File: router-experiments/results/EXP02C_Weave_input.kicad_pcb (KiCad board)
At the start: 2 copper layers, 45.4 x 45.4 mm, 144 parts

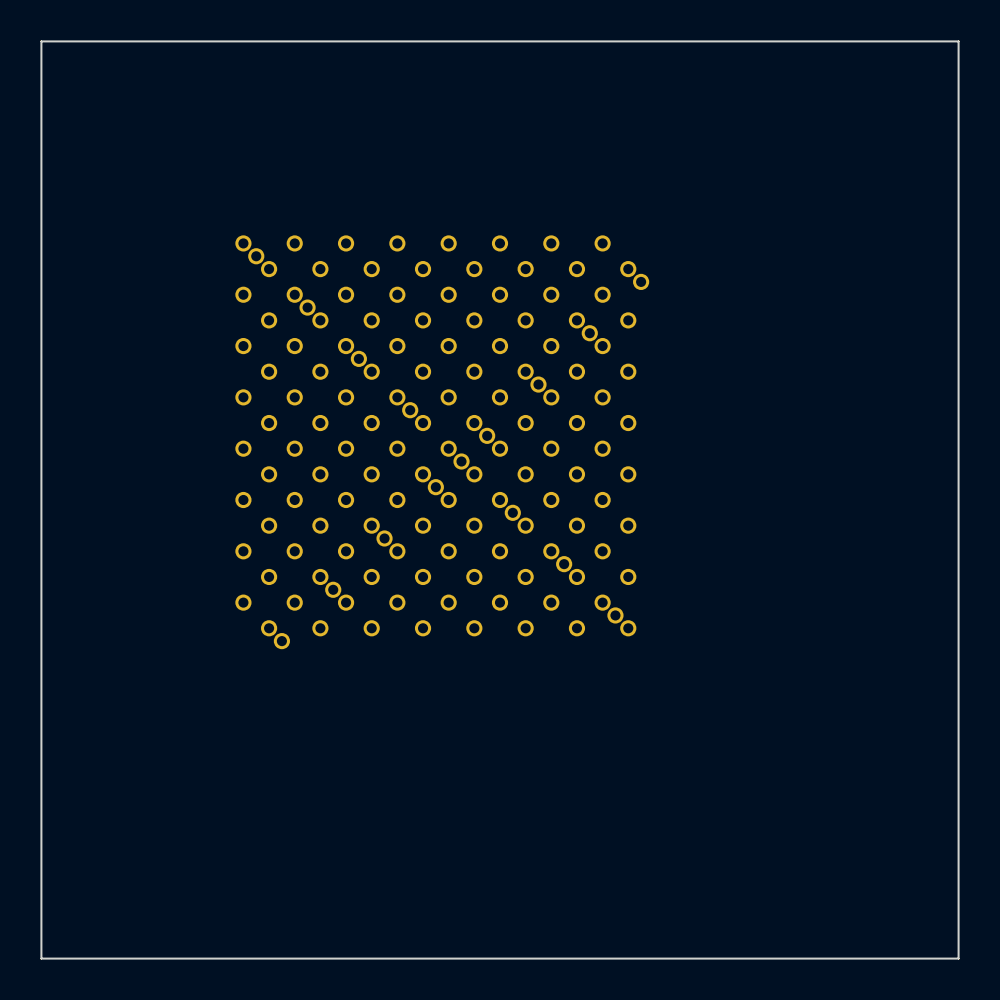
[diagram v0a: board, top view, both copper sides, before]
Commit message: feat(router-v5): Verify high-density routing strategies for BGA/THT grids - **Experiment Findings**: Confirmed that 'Center Escape' (Tunneling/Surface) fails in 100% saturated grids due to 'Via Forests' or channel blocking. - **Solution**: Validated 'Perimeter Routing' (Escape to edge) and 'Channel Reservation' (depopulation) as the only robust strategies for standard technology (no HDI). - **Core Update**: Updated MazeRouter to support Strict Layer Partitioning (Manhattan Topology) and 4-Layer routing (L2/L3 utilization). - **Bug Fixes**: Fixed component blockage margin logic, improved conflict reporting, and fixed kiutils serialization for SMD pads. - **Documentation**: Updated docs/router/fanout_pass_results.md with definitive findings on 'The Via Forest Barrier' and recommended escape strategies.
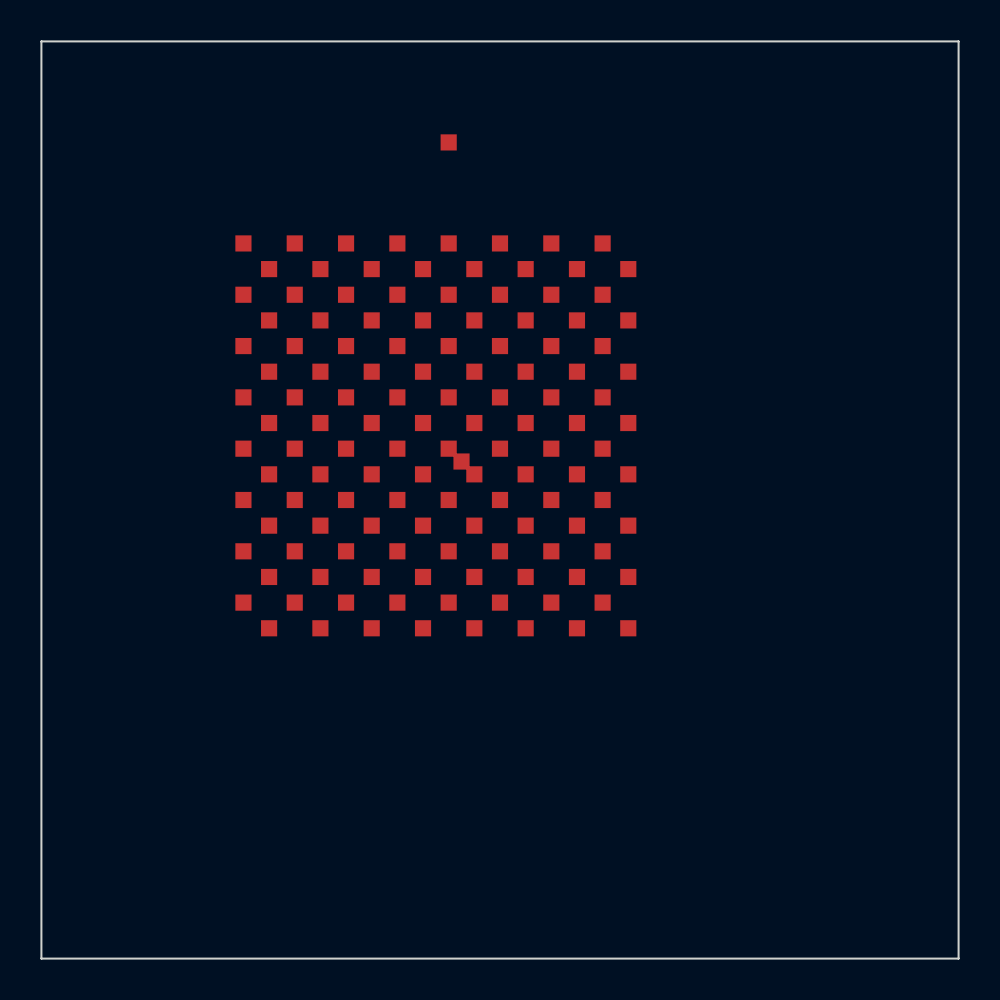
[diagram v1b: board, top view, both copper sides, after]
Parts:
- removed D1_0, D1_1, D1_2, D1_3, D1_4, D1_5, D1_6, D1_7, D2_0, D2_1, D2_2, D2_3, D2_4, D2_5, D2_6, D2_7: Pin, Test:Pin
- added ESC_Center: Pin, Test:Pin, F.Cu at (20.8, 20.8)
- added ESC_North: Pin, Test:Pin, F.Cu at (20.2, 5.00)
